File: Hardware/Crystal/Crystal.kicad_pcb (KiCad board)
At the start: 2 copper layers, 66 x 43 mm, 46 parts, among them J1 USB_B_Micro, U1 AP63205WU, U2 NCP1117-3.3_SOT223, U3 ESP32-C3-WROOM-02, U4 TXS0102DCT, U5 TXS0108EPW

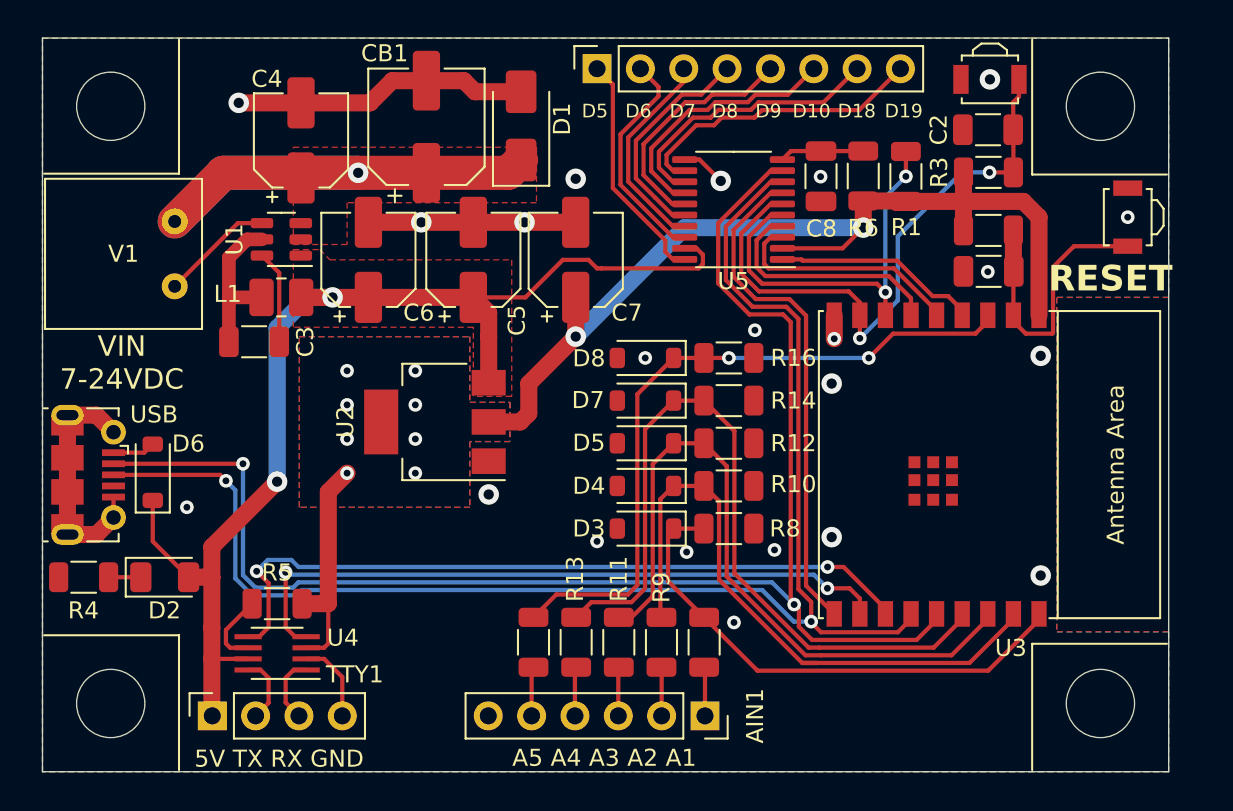
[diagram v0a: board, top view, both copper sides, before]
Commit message: Revised L1 for possible 2A output, cleaner fill zones
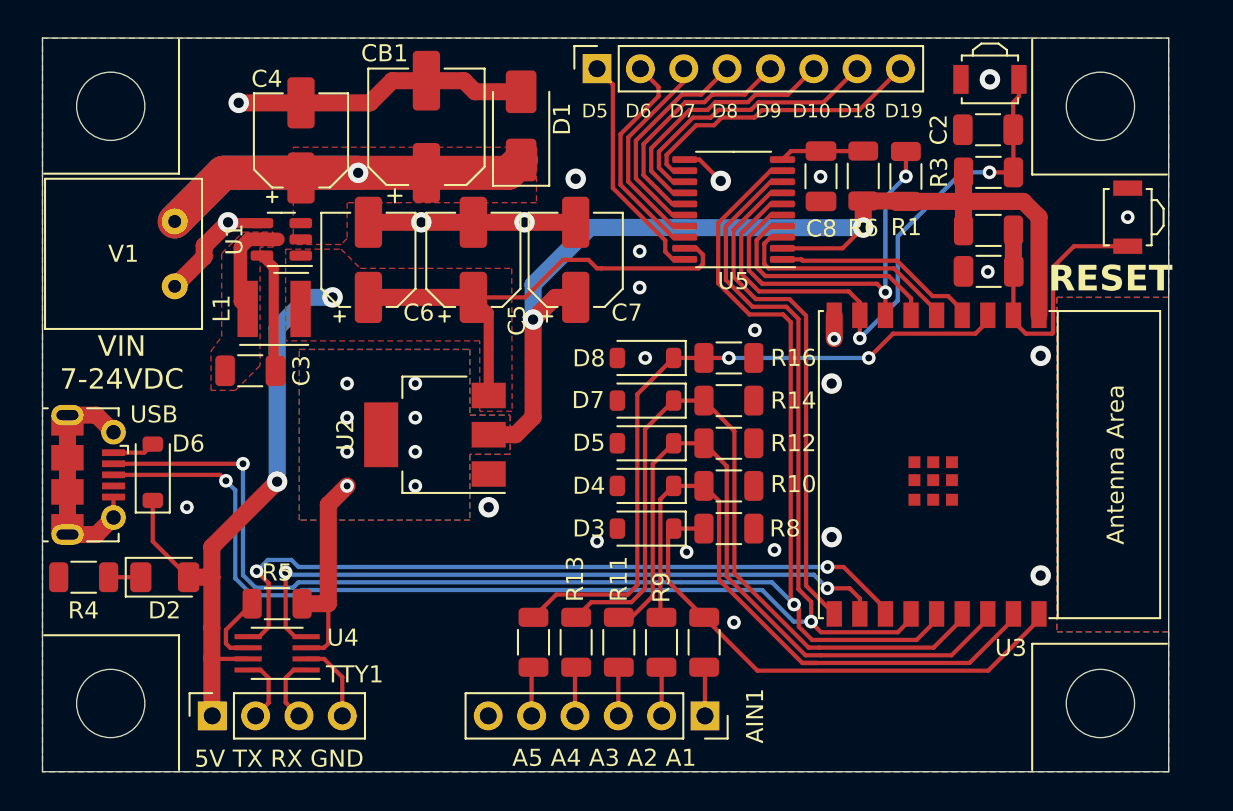
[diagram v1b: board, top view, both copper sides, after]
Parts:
- L1: footprint Inductor_SMD:L_1008_2520Metric_Pad1.43x2.20mm_HandSolder -> Inductor_SMD_Wurth:L_Wurth_WE-LQSH-4020
- moved C3 1.71 mm to (32.2, 39.5)
- moved L1 0.80 mm to (33.6, 35.9)
- moved U2 0.75 mm to (43.0, 43.2)
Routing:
- net +3.3V: track 70.0 -> 73.9 mm
- net +5V: track 69.1 -> 65.9 mm
- net Net-(U1-SW): track 9.23 -> 6.16 mm
- net Net-(U1-BST): track 5.47 -> 7.08 mm
- net GND: track 59.4 -> 59.8 mm, vias 22 -> 25
- added copper zone on F.Cu, net Net-(U1-SW)
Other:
- board text added: "Antenna Area"

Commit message: Checkpoint
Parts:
- added D9: Blue, LED_SMD:LED_1206_3216Metric, F.Cu at (32.1, 55.6)
- added R17: 1k, Resistor_SMD:R_1206_3216Metric, F.Cu at (32.1, 50.8)
- D2: value LED -> Red
- L1: footprint Inductor_SMD_Wurth:L_Wurth_WE-LQSH-4020 -> Inductor_SMD:L_1008_2520Metric_Pad1.43x2.20mm_HandSolder
- moved U4 2.88 mm to (36.6, 55.7)
- moved R5 2.88 mm to (36.6, 52.8)
- moved C3 1.71 mm to (32.4, 37.8)
- moved L1 0.80 mm to (34.0, 35.2)
- moved U2 0.75 mm to (43.0, 42.5)
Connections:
- J1 pad 2: /GPIO19 -> /USB_D+
- J1 pad 3: /GPIO18 -> /USB_D-
- U3 pad 13: /GPIO18 -> /USB_D-
- U3 pad 14: /GPIO19 -> /USB_D+
- U5 pad 8: /GPIO18 -> unconnected-(U5-A7-Pad8)
- U5 pad 9: /GPIO19 -> unconnected-(U5-A8-Pad9)
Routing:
- net /GPIO19: track 88.4 -> 0.00 mm, vias 2 -> 0
- net /GPIO18: track 85.3 -> 0.00 mm, vias 2 -> 0
- net /USB_D+: track 0.00 -> 55.6 mm, vias 0 -> 2
- net /USB_D-: track 0.00 -> 52.0 mm, vias 0 -> 2
- net +5V: track 65.9 -> 76.8 mm
- net +3.3V: track 73.9 -> 68.4 mm
- net GND: track 59.8 -> 56.7 mm, vias 25 -> 24
- net Net-(U1-SW): track 6.16 -> 9.23 mm
- net /RXD: track 39.8 -> 37.0 mm
- net /TXD: track 43.6 -> 40.9 mm
- net Net-(D9-K): track 0.00 -> 1.95 mm
- net Net-(D9-A): track 3.93 -> 5.84 mm
- net Net-(U1-BST): track 7.08 -> 5.47 mm
- net Net-(TTY1-Pin_3): track 3.94 -> 5.37 mm
- net Net-(U4-OE): track 4.38 -> 4.98 mm
- removed copper zone on F.Cu, net Net-(U1-SW)
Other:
- board text added: "+"
- board text added: "-"
- board text added: "7-24VDC"
- board text removed: "Antenna Area"
- board text removed: "VIN 7-24VDC"

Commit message: Final cleanup, added tags for JLCPCB Fabrication
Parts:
- CB1: footprint Capacitor_SMD:CP_Elec_6.3x7.7 -> Capacitor_THT:CP_Radial_D6.3mm_P2.50mm
- moved CB1 1.33 mm to (42.0, 26.4)
- moved C4 1.15 mm to (34.0, 26.0)
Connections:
- J1 pad 2: /USB_D+ -> /USB_D-
- J1 pad 3: /USB_D- -> /USB_D+
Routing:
- net GND: track 56.7 -> 57.4 mm, vias 24 -> 30
- added copper zone on B.Cu, net +12V
- added copper zone on B.Cu, net +5V
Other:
- board text added: "JLCJLCJLCJLC"

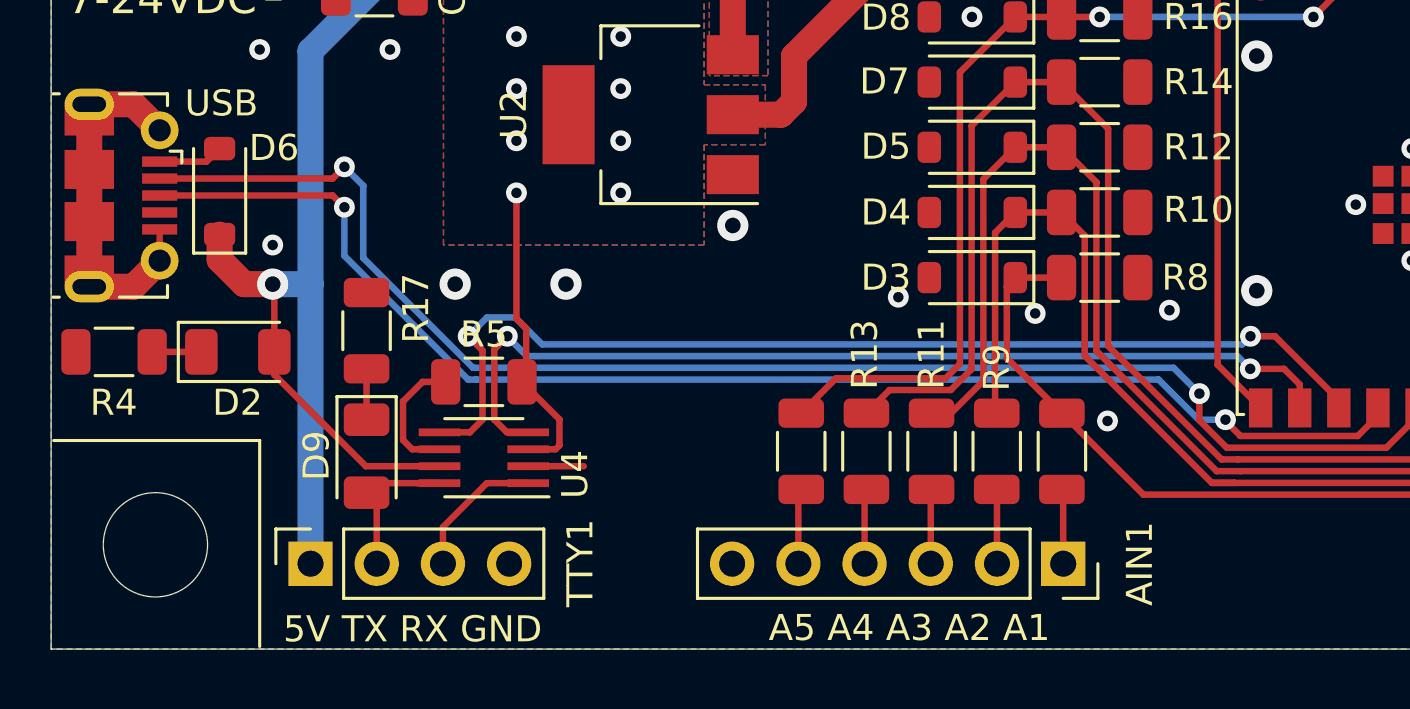
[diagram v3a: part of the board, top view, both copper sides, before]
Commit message: Swap TX and RX pins on COM port, populate PCBA data in KiCad
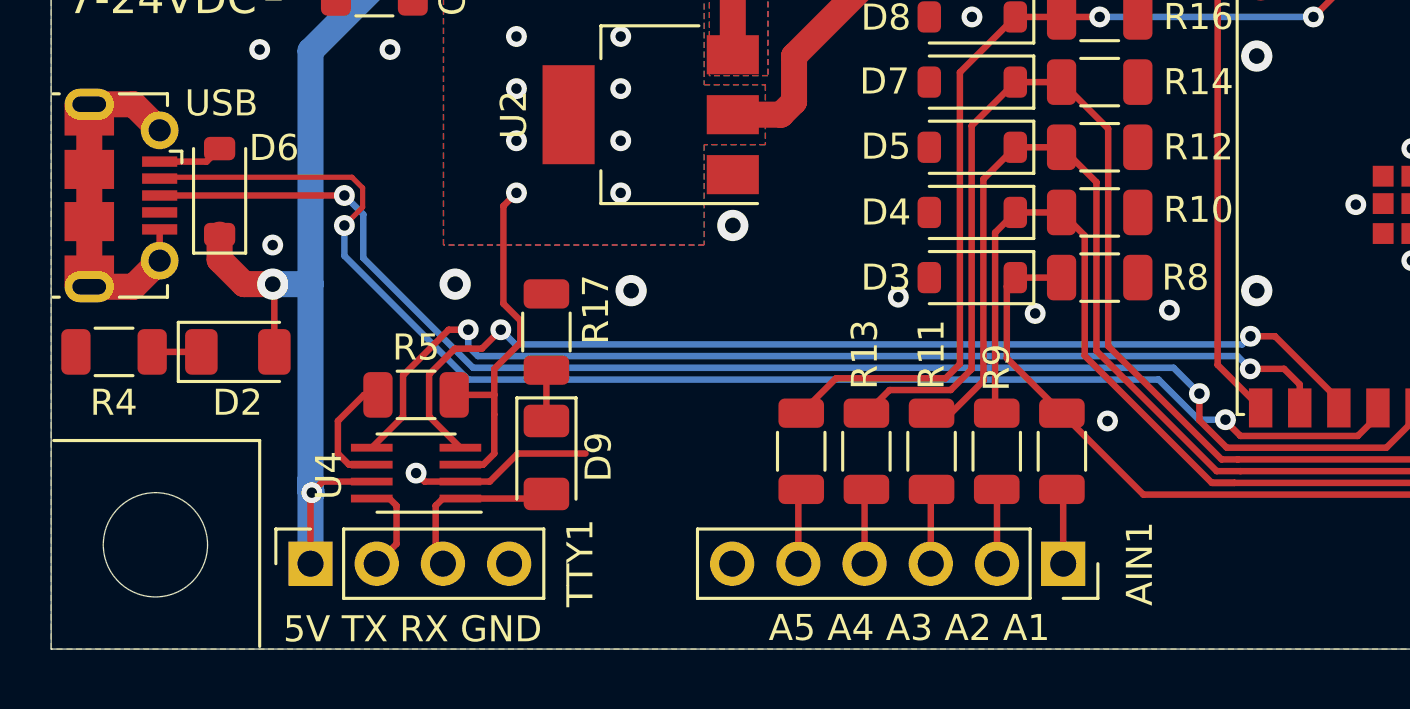
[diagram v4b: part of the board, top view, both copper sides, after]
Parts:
- moved D9 6.90 mm to (39.0, 55.6)
- moved R17 6.90 mm to (39.0, 50.8)
- moved U4 2.67 mm to (34.0, 56.2)
- moved R5 2.65 mm to (34.0, 53.2)
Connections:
- TTY1 pad 2: Net-(D9-A) -> Net-(TTY1-Pin_2)
- TTY1 pad 3: Net-(TTY1-Pin_3) -> Net-(D9-A)
- U4 pad 1: Net-(TTY1-Pin_3) -> Net-(D9-A)
- U4 pad 4: /RXD -> /TXD
- U4 pad 5: /TXD -> /RXD
- U4 pad 8: Net-(D9-A) -> Net-(TTY1-Pin_2)
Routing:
- net Net-(TTY1-Pin_3): track 5.37 -> 0.00 mm
- net GND: track 57.4 -> 62.4 mm, vias 30 -> 31
- net Net-(TTY1-Pin_2): track 0.00 -> 3.60 mm
- net /RXD: track 37.0 -> 40.5 mm
- net +5V: track 76.8 -> 73.8 mm, vias 2 -> 3
- net +3.3V: track 68.4 -> 70.5 mm
- net /USB_D-: track 52.0 -> 53.7 mm
- net /USB_D+: track 55.6 -> 54.3 mm
- net Net-(D9-A): track 5.84 -> 6.78 mm

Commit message: Further board cleanup
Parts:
- BOOT1, RESET1: footprint Button_Switch_SMD:SW_SPST_B3U-3000P -> Button_Switch_SMD:SW_SPST_B3U-3000P-B
- GPIO1: value Conn_01x08_Female -> Conn_01x06; footprint Connector_PinSocket_2.54mm:PinSocket_1x08_P2.54mm_Vertical -> Connector_PinSocket_2.54mm:PinSocket_1x06_P2.54mm_Vertical
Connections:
- U5 pad 12: Net-(GPIO1-Pin_8) -> unconnected-(U5-B8-Pad12)
- U5 pad 13: Net-(GPIO1-Pin_7) -> unconnected-(U5-B7-Pad13)
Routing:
- net Net-(GPIO1-Pin_8): track 17.6 -> 0.00 mm
- net Net-(GPIO1-Pin_7): track 16.4 -> 0.00 mm
- net Net-(GPIO1-Pin_6): track 15.3 -> 16.2 mm
- net Net-(GPIO1-Pin_5): track 14.2 -> 15.1 mm
- net Net-(GPIO1-Pin_4): track 13.1 -> 13.7 mm
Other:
- board text added: "5V RX TX GND"
- board text added: "BOOT"
- board text removed: "5V TX RX GND"
- board text removed: "D18"
- board text removed: "D19"

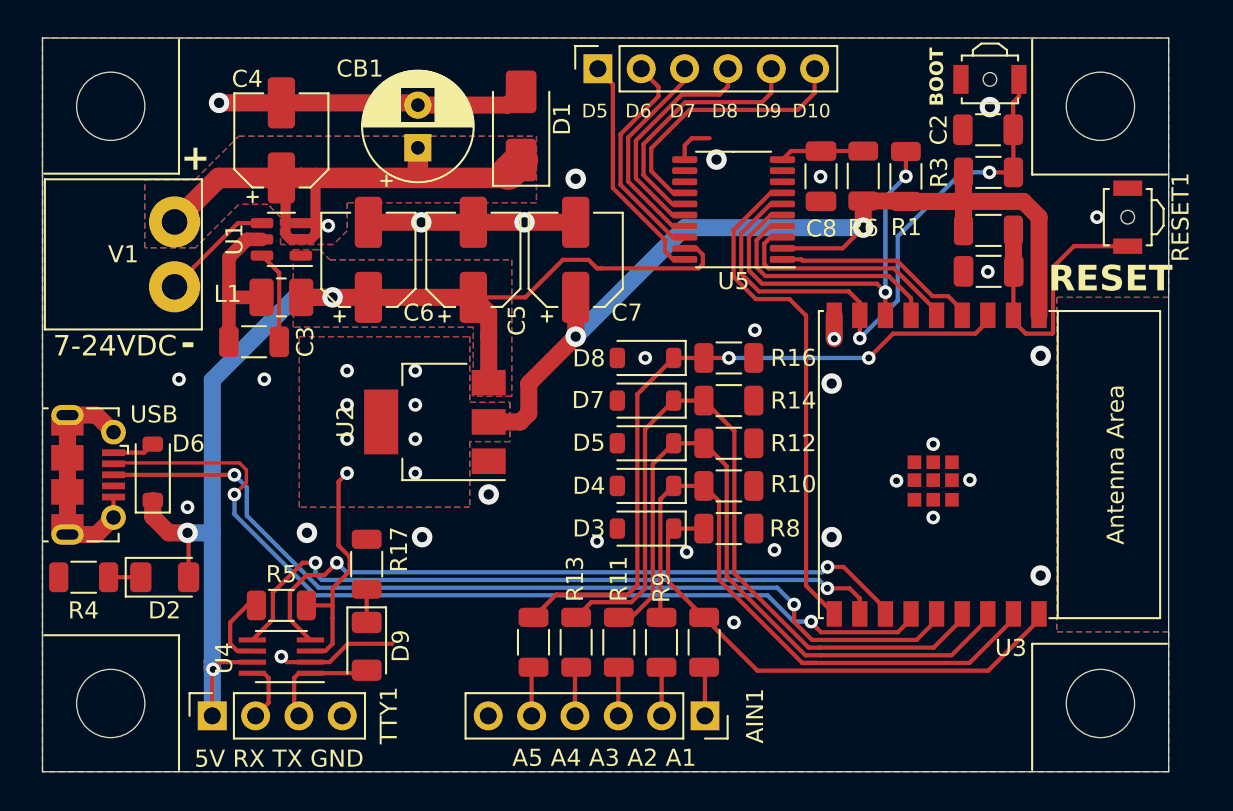
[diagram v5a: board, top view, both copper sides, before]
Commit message: Changed mounting holes to be drilled and plated instead of milled.
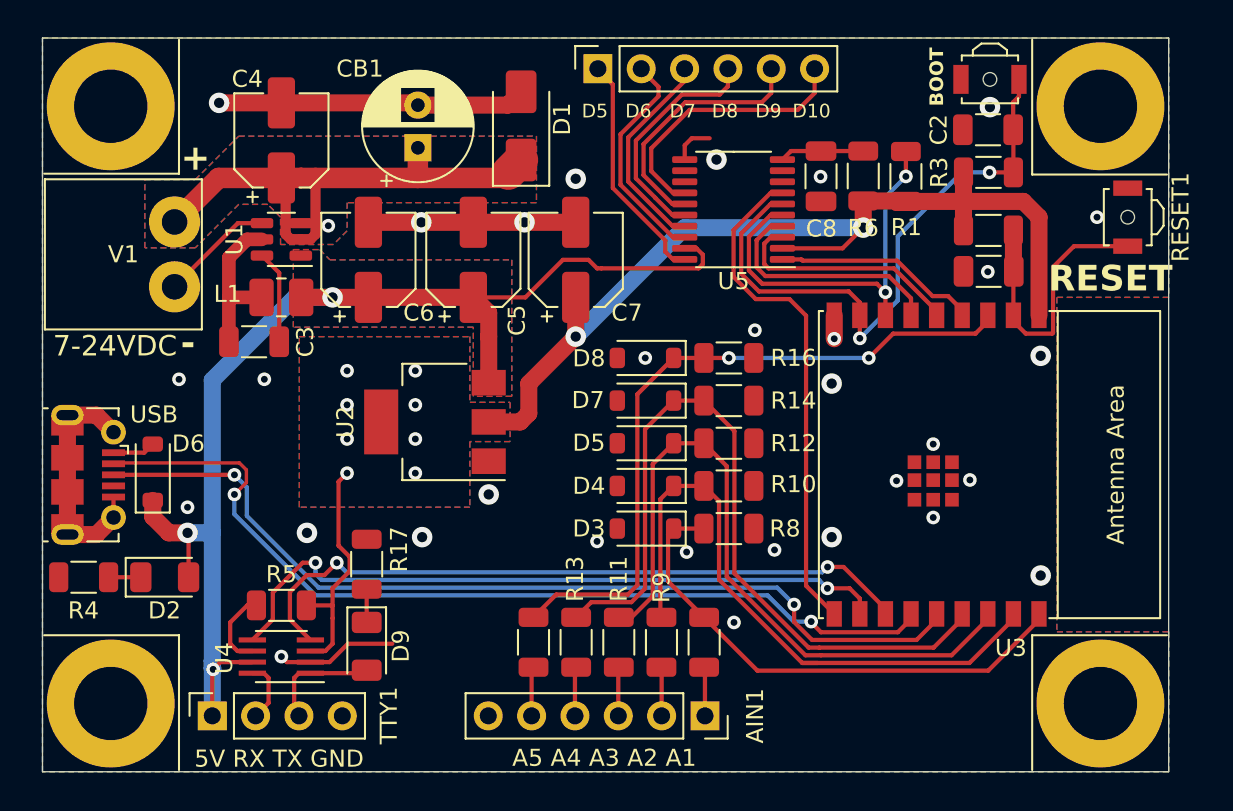
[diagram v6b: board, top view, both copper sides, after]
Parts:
- added REF**: MountingHole_4.3mm_M4_DIN965_Pad, MountingHole:MountingHole_4.3mm_M4_DIN965_Pad, F.Cu at (82.0, 59.0)
- added REF**: MountingHole_4.3mm_M4_DIN965_Pad, MountingHole:MountingHole_4.3mm_M4_DIN965_Pad, F.Cu at (82.0, 24.0)
- added REF**: MountingHole_4.3mm_M4_DIN965_Pad, MountingHole:MountingHole_4.3mm_M4_DIN965_Pad, F.Cu at (24.0, 59.0)
- added REF**: MountingHole_4.3mm_M4_DIN965_Pad, MountingHole:MountingHole_4.3mm_M4_DIN965_Pad, F.Cu at (24.0, 24.0)
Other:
- outline, holes or cut-outs redrawn

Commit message: PCB Revision for 5mm power plug to match EX-8874
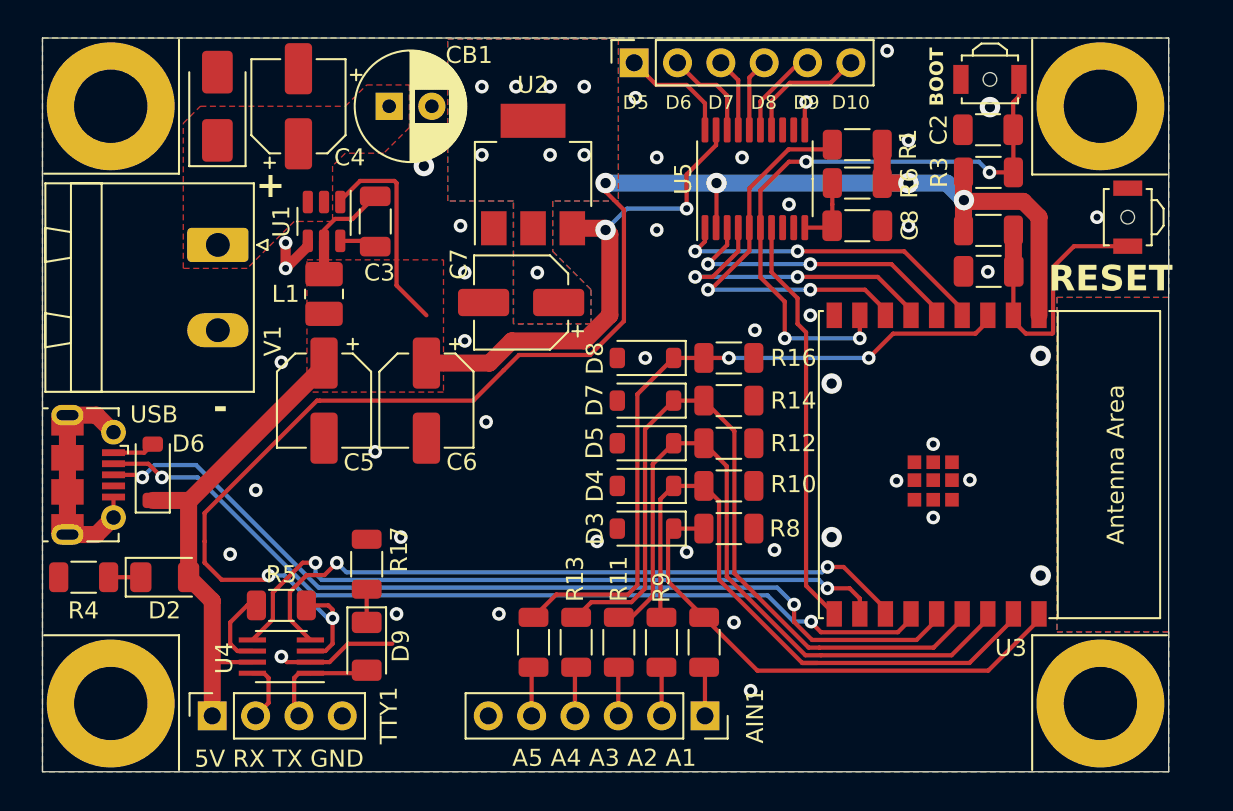
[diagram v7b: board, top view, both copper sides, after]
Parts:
- V1: footprint Terminal_Wuerth_new:WR-TBL 2P -> Connector_Phoenix_MSTB:PhoenixContact_MSTBA_2,5_2-G_1x02_P5.00mm_Horizontal
- moved D1 17.8 mm to (30.2, 24.0)
- moved U2 15.6 mm to (48.8, 28.0), turned to 90 degrees
- moved C5 12.0 mm to (36.5, 41.2), turned to -90 degrees
- moved C3 10.0 mm to (39.5, 30.8), turned to 90 degrees
- moved C6 8.92 mm to (42.5, 41.2), turned to -90 degrees
- moved V1 5.57 mm to (30.3, 32.1)
- moved C7 4.06 mm to (48.0, 35.5), turned to 180 degrees
- moved C8 3.60 mm to (67.8, 31.0), turned to 0 degrees
- moved R1 3.40 mm to (67.8, 26.2), turned to 180 degrees
- moved CB1 2.96 mm to (40.3, 24.0), turned to 0 degrees
- moved U1 2.71 mm to (36.5, 30.8), turned to -90 degrees
- moved L1 2.51 mm to (36.5, 35.0), turned to -90 degrees
- moved C4 2.24 mm to (35.0, 24.0)
- moved U5 2.19 mm to (61.8, 28.2), turned to 90 degrees
- moved GPIO1 2.15 mm to (54.7, 21.4)
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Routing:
- net GND: track 62.2 -> 26.8 mm, vias 31 -> 43
- net +12V: track 33.4 -> 0.00 mm, vias 1 -> 0
- net +3.3V: track 70.5 -> 96.7 mm, vias 10 -> 14
- net Net-(GPIO1-Pin_5): track 15.1 -> 5.37 mm
- net Net-(GPIO1-Pin_4): track 13.7 -> 4.30 mm
- net Net-(GPIO1-Pin_6): track 16.2 -> 7.27 mm
- net Net-(GPIO1-Pin_3): track 12.4 -> 4.36 mm
- net Net-(GPIO1-Pin_2): track 13.2 -> 5.72 mm
- net Net-(GPIO1-Pin_1): track 13.7 -> 6.70 mm
- net /GPIO5: track 12.1 -> 19.0 mm, vias 0 -> 2
- net /GPIO10: track 29.9 -> 24.2 mm
- net /GPIO7: track 14.2 -> 18.3 mm, vias 0 -> 2
- net /GPIO6: track 13.9 -> 17.5 mm, vias 0 -> 2
- net Net-(U1-SW): track 9.23 -> 5.77 mm
- net Net-(U1-BST): track 5.47 -> 2.19 mm
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- removed copper zone on B.Cu, net +12V
- removed copper zone on B.Cu, net +5V
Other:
- board text removed: "7-24VDC"
